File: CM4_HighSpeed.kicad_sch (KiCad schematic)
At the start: 7 parts, among them J10 Conn_01x22_Female, J11 690-019-298-412, J9 Conn_01x22_Female, U7 RT9742SNGV

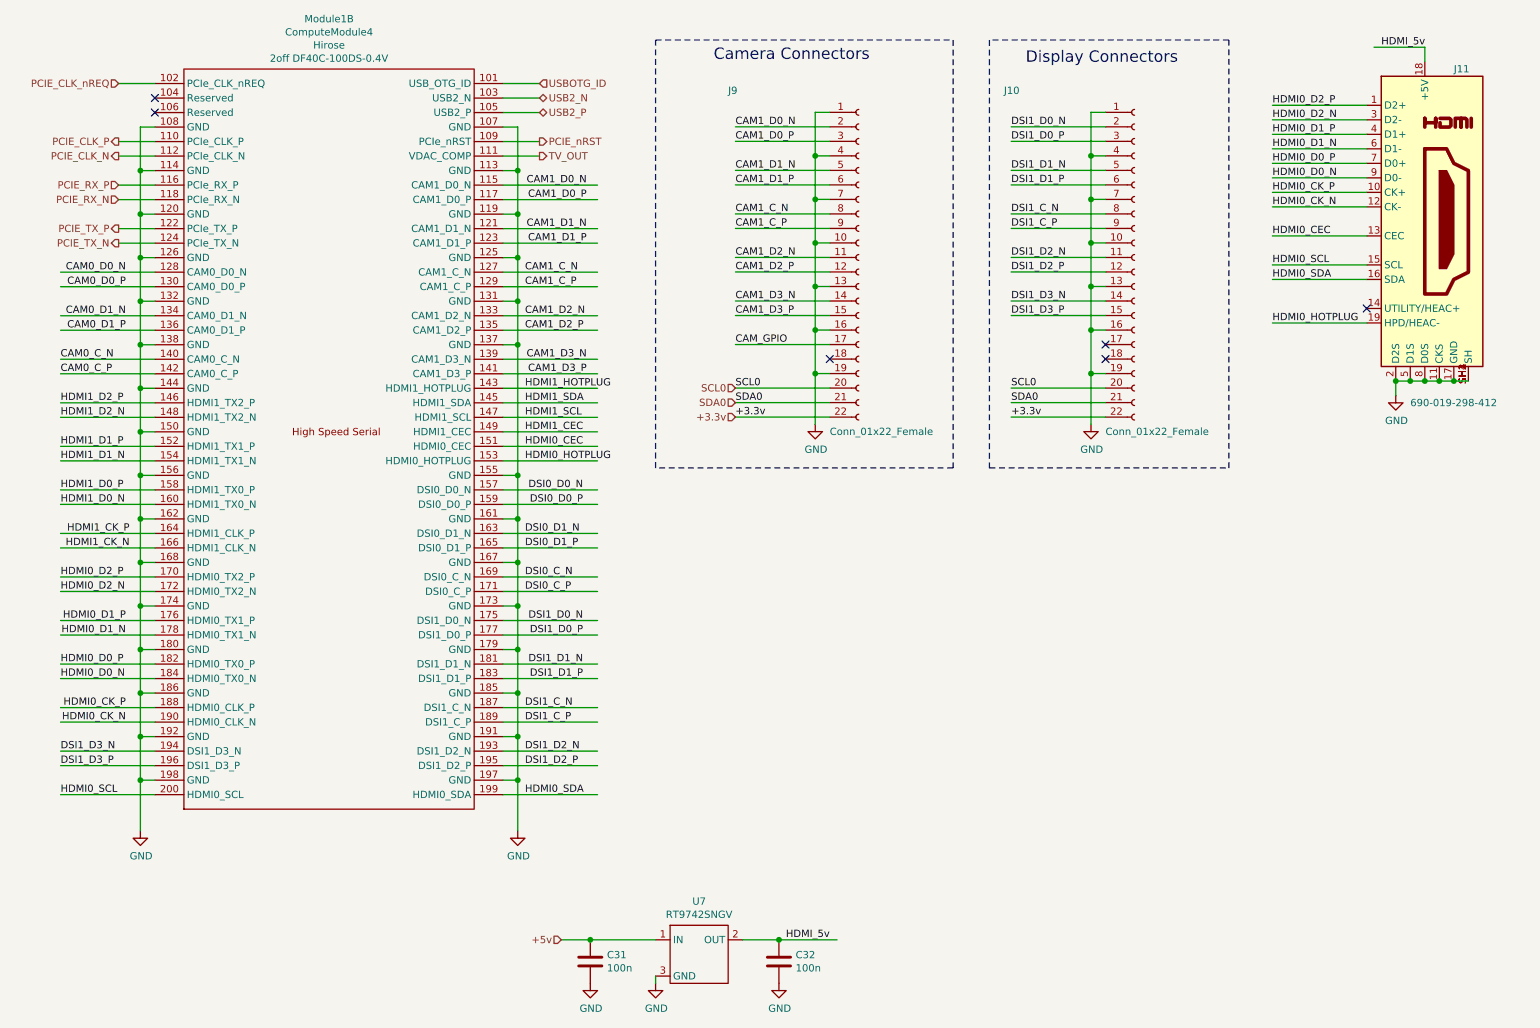
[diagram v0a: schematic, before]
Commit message: Initial layout and all parts added. Some pins still not connected to power
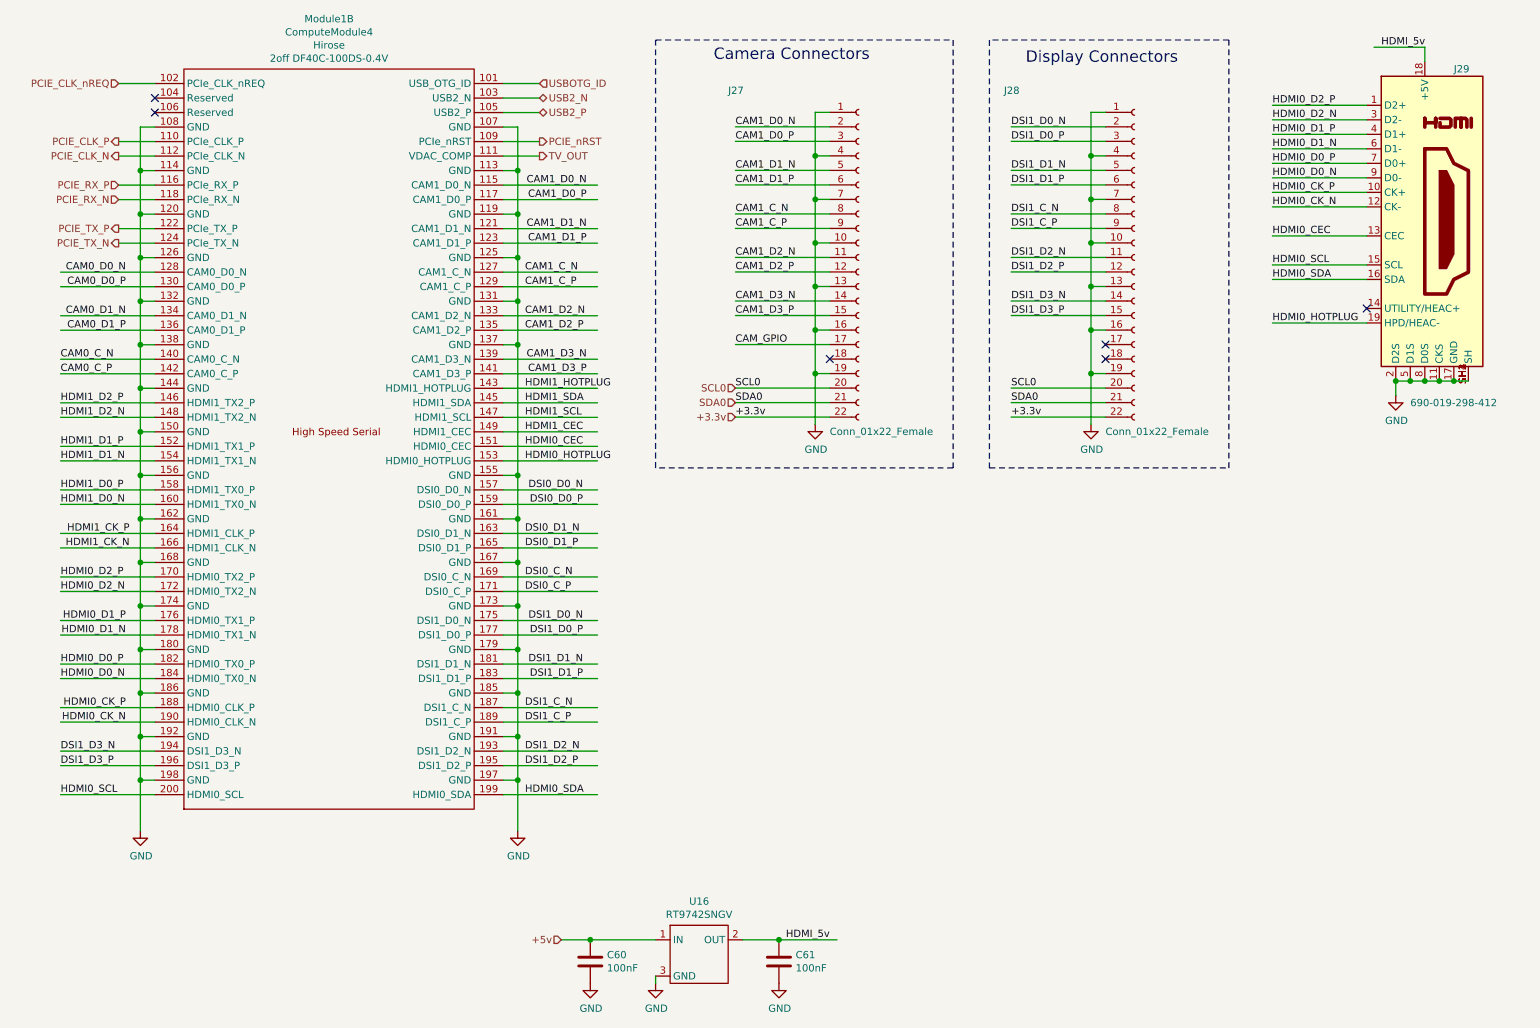
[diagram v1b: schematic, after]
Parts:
- C60: renamed from C31; value 100n -> 100nF
- C61: renamed from C32; value 100n -> 100nF
- renumbered J9 to J27, J10 to J28, J11 to J29, U7 to U16
